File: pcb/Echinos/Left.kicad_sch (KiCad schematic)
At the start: 39 parts, among them J1 USB_C_Receptacle_USB2.0, J2 TagConnect_6pins, J206 Conn_01x06_Pin, J208 FPC (PCB), J301 SATA-7p, J4 FPC_VIK, SW1 SW_Push, SW2 SW_Push, U2 W25Q128JVS, U3 ESD7L5.0DT5G-N, U5 XC6210B332MR-G, U7 D3V3F4U6S-7

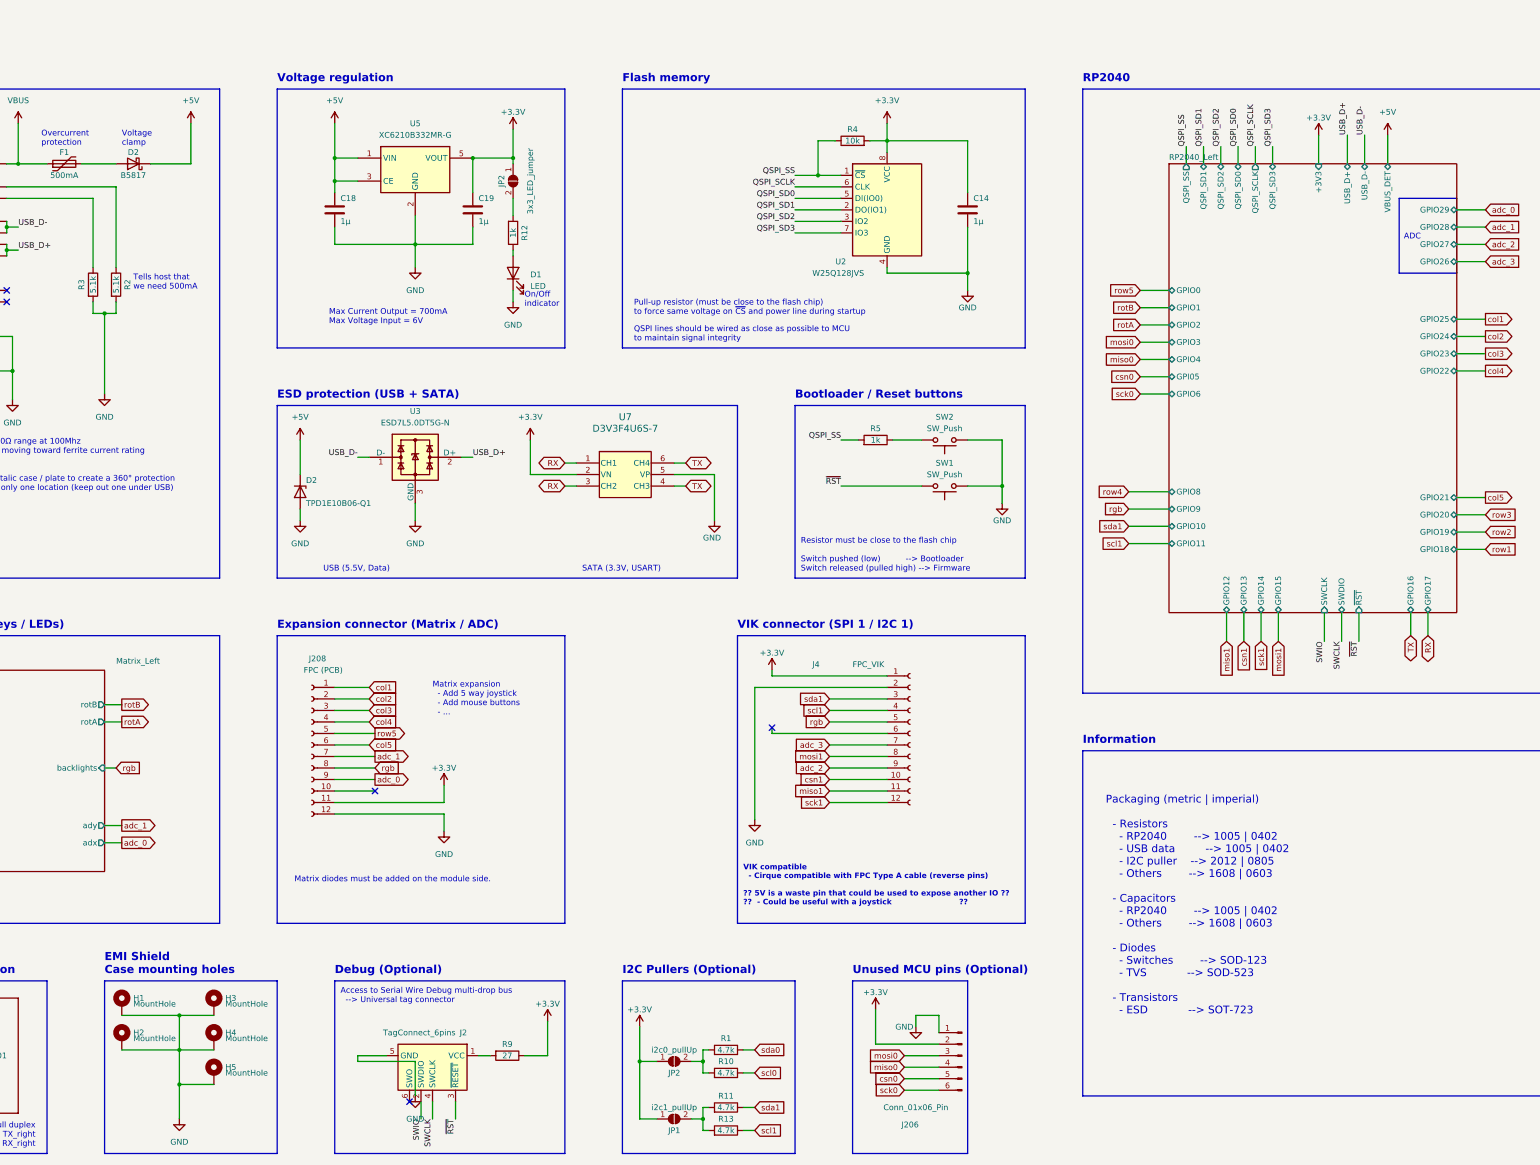
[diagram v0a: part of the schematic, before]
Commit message: 🚧 [PCB] - Backup before trying to add 5.0V support.
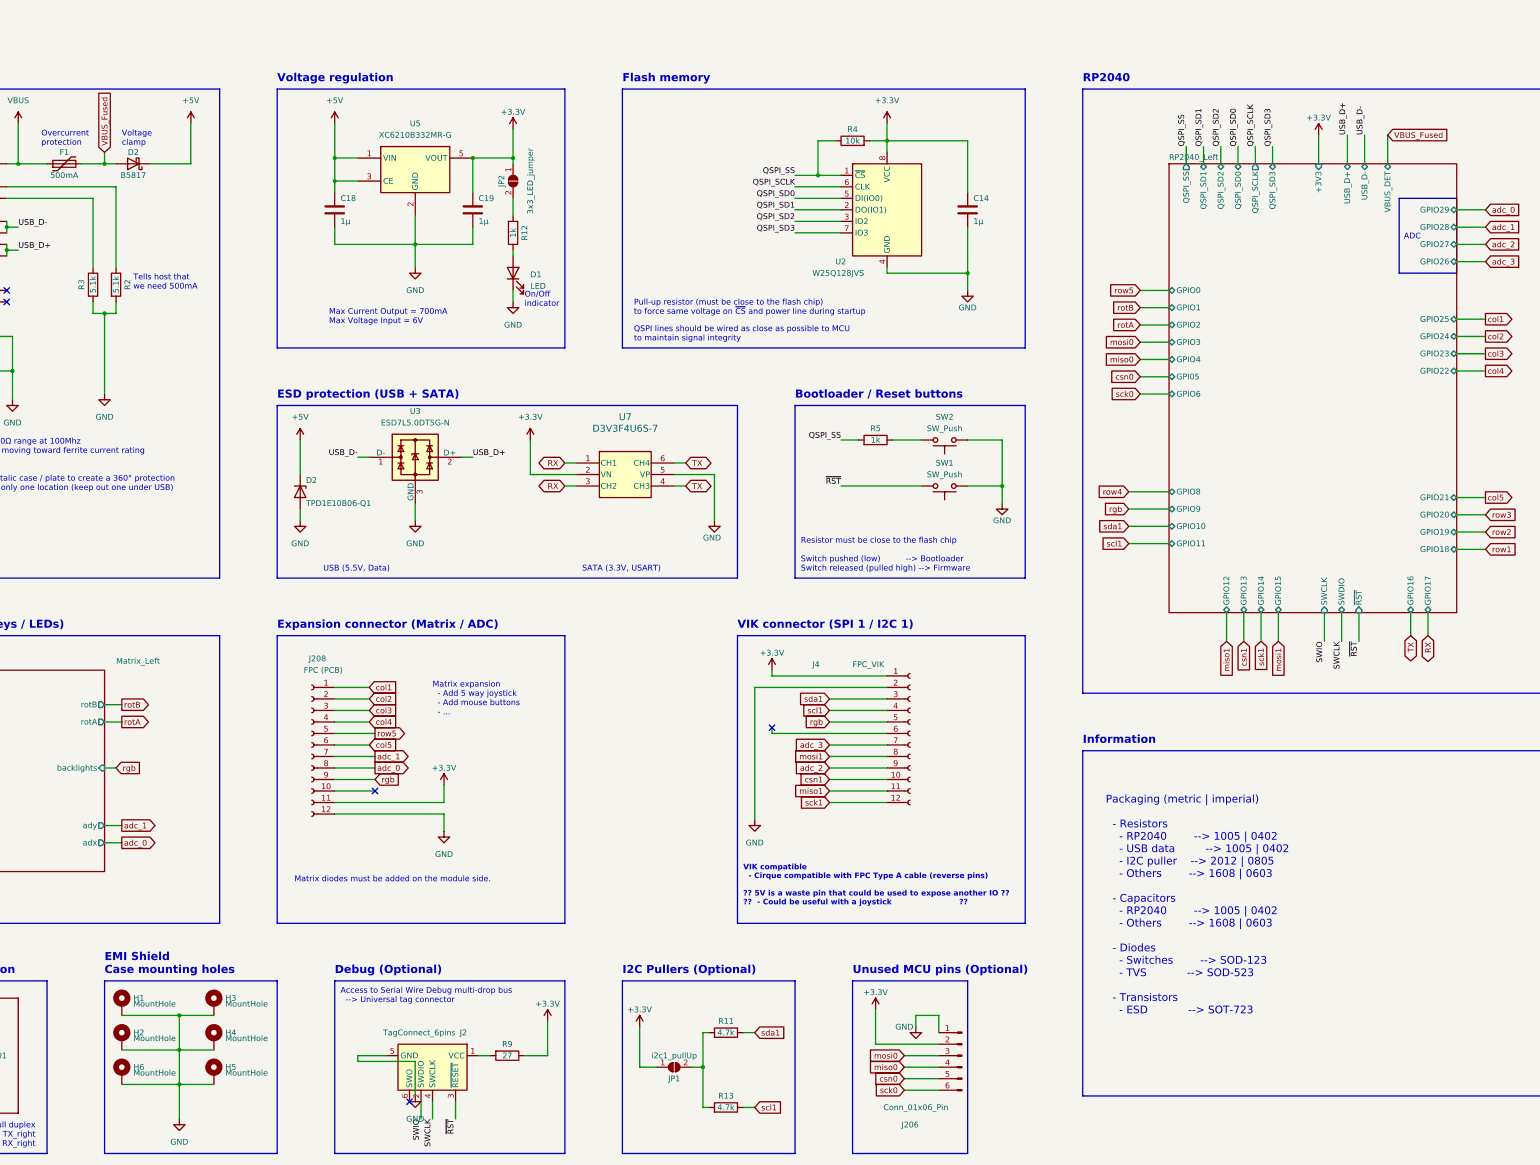
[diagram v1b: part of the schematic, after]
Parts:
- removed JP2: i2c0_pullUp, Echinos:SolderJumper_Open_0.8x1.2mm, symbol Jumper:SolderJumper_2_Open
- removed R1, R10: 4.7k, Resistor_SMD:R_0805_2012Metric_Pad1.20x1.40mm_HandSolder, symbol Device:R
- added H6: MountHole, Echinos:MountingHole_3mm_Pad_Via, symbol Mechanical:MountingHole_Pad
- J206: footprint Connector_PinHeader_2.54mm:PinHeader_1x06_P2.54mm_Vertical -> Connector_PinSocket_2.00mm:PinSocket_1x06_P2.00mm_Horizontal; now left out of the parts list
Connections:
- net GND: now also H6.1
- net adc_0: now also J208.8 (Pin_8); no longer J208.9 (Pin_9)
- net rgb: now also J208.9 (Pin_9); no longer J208.8 (Pin_8)
- net VBUS_Fused: now reaches D2.2 (A), F1.2
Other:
- moved on the sheet: JP1, R11, R13

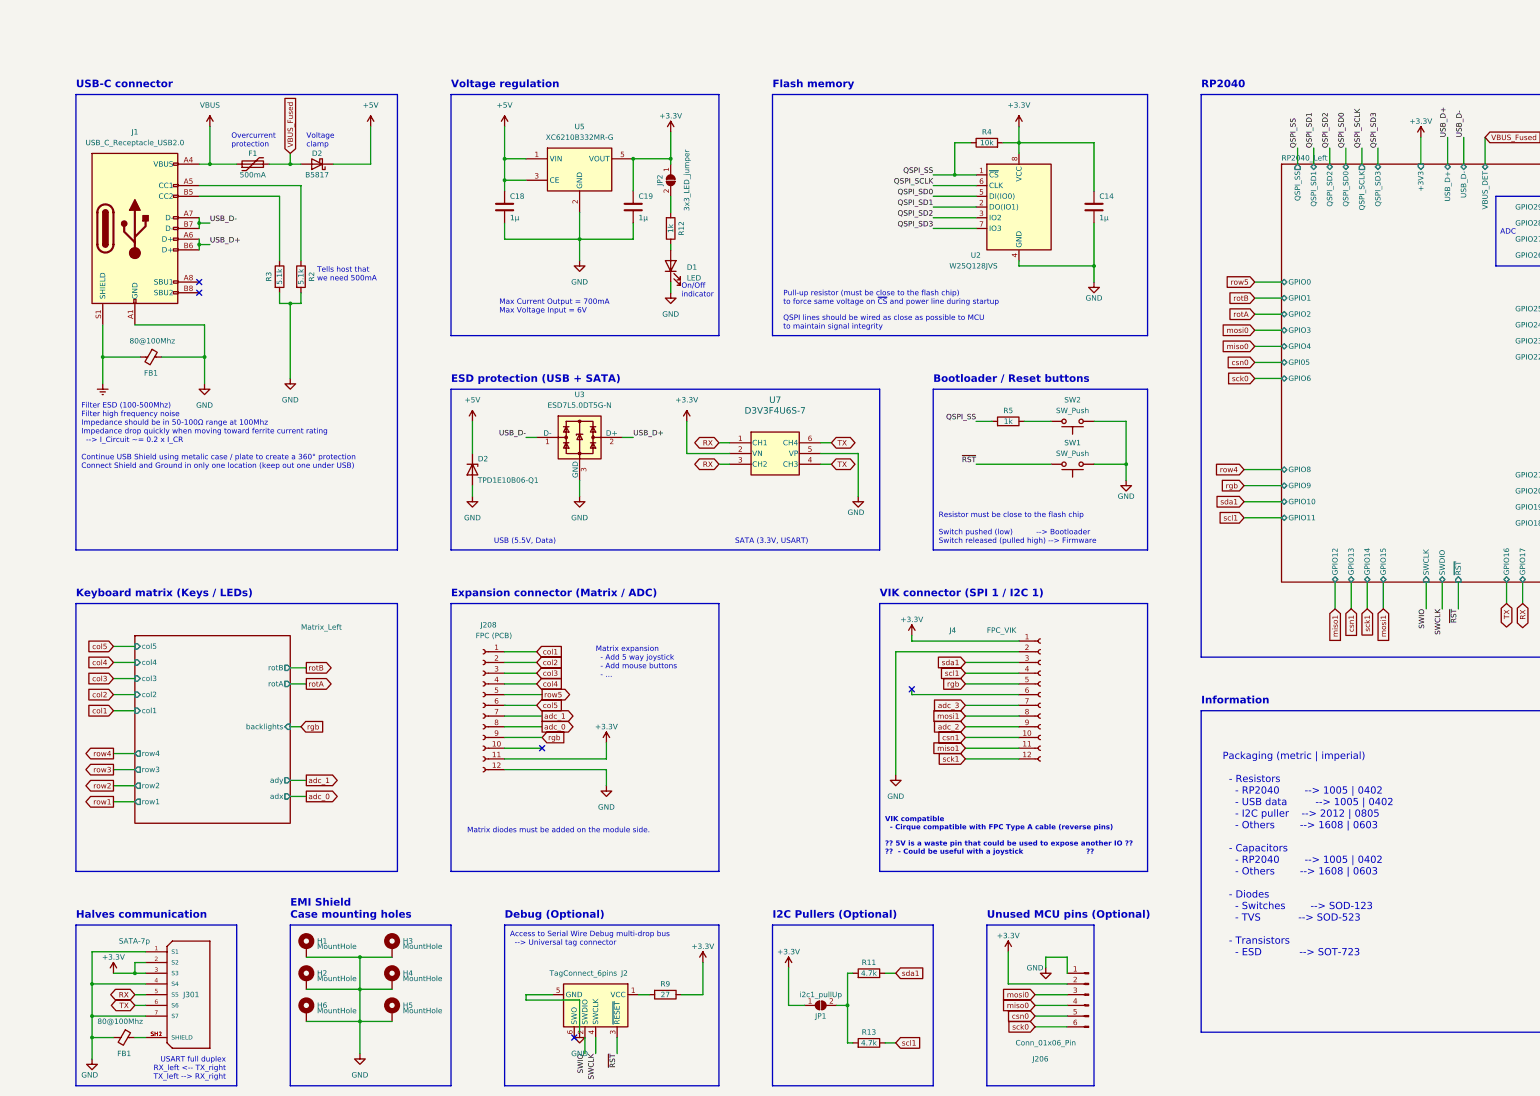
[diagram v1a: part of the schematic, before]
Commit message: ✨ 🚧 [PCB] - Halves are now connected with 5.0V power to be able to expose it to modules (see VIK standard). Update the whole routing to make this happens. VBUS and 5.0V are now split with a schottky diode to still be able to detect when USB is plugged but avoid reverse current in case power comes from the other half. Add ESD events protection to SATA connector.
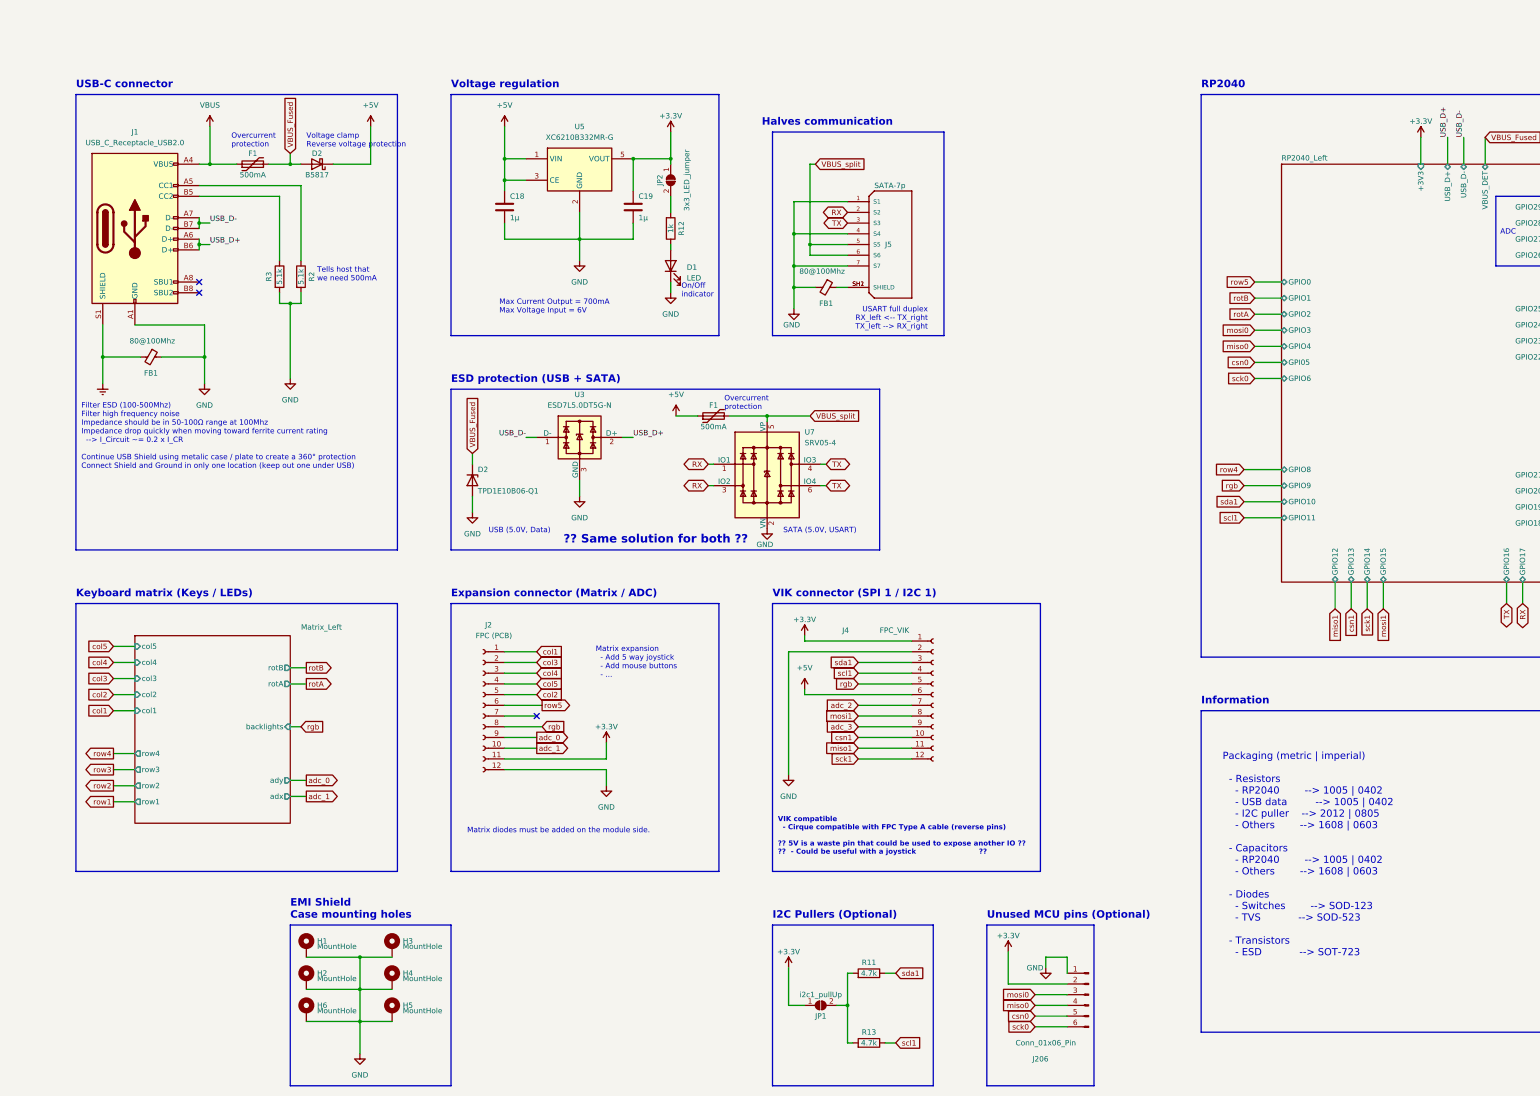
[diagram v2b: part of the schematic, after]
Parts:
- removed C14: 1µ, Capacitor_SMD:C_0603_1608Metric_Pad1.08x0.95mm_HandSolder, symbol Device:C
- removed J2: TagConnect_6pins, Connector:Tag-Connect_TC2030-IDC-FP_2x03_P1.27mm_Vertical, symbol Connector:Conn_ARM_SWD_TagConnect_TC2030
- removed R4: 10k, Resistor_SMD:R_0402_1005Metric_Pad0.72x0.64mm_HandSolder, symbol Device:R
- removed R5: 1k, Resistor_SMD:R_0402_1005Metric_Pad0.72x0.64mm_HandSolder, symbol Device:R
- removed R9: 27, Resistor_SMD:R_0402_1005Metric_Pad0.72x0.64mm_HandSolder, symbol Device:R
- removed SW1, SW2: SW_Push, Button_Switch_SMD:SW_SPST_CK_KXT3, symbol Switch:SW_Push
- removed U2: W25Q128JVS, Package_SO:SOIC-8_5.23x5.23mm_P1.27mm, symbol Memory_Flash:W25Q128JVS
- removed U7: D3V3F4U6S-7, Echinos:D_TVS_SOT-363, symbol Echinos:D3V3F4U6S-7
- added F1: 500mA, Fuse:Fuse_0603_1608Metric_Pad1.05x0.95mm_HandSolder, symbol Device:Polyfuse
- added U7: SRV05-4, Package_TO_SOT_SMD:SOT-23-6, symbol Power_Protection:SRV05-4
- renumbered J208 to J2, J301 to J5
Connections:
- net +3.3V: no longer J5.2 (S2), J5.3 (S3)
- net +5V: now also J4.6 (Pin_6), F1.1; no longer D2.1 (K)
- net GND: now also U7.2 (VN)
- net RX: now also J5.2 (S2), U7.1 (IO1), U7.3 (IO2); no longer J5.5 (S5)
- net TX: now also J5.3 (S3), U7.4 (IO3), U7.6 (IO4); no longer J5.6 (S6)
- net VBUS_Fused: now also D2.1 (K)
- net adc_0: now also J2.9 (Pin_9); no longer J2.8 (Pin_8)
- net adc_1: now also J2.10 (Pin_10); no longer J2.7 (Pin_7)
- net adc_2: now also J4.7 (Pin_7); no longer J4.9 (Pin_9)
- net adc_3: now also J4.9 (Pin_9); no longer J4.7 (Pin_7)
- net col2: now also J2.5 (Pin_5); no longer J2.2 (Pin_2)
- net col3: now also J2.2 (Pin_2); no longer J2.3 (Pin_3)
- net col4: now also J2.3 (Pin_3); no longer J2.4 (Pin_4)
- net col5: now also J2.4 (Pin_4); no longer J2.6 (Pin_6)
- net rgb: now also J2.8 (Pin_8); no longer J2.9 (Pin_9)
- net row5: now also J2.6 (Pin_6); no longer J2.5 (Pin_5)
- new net VBUS_split: F1.2, J5.5 (S5), J5.6 (S6), U7.5 (VP)
- no-connect marks 5 -> 3
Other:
- sheet RP2040_Left ports: added none; removed QSPI_SCLK, QSPI_SD0, QSPI_SD1, QSPI_SD2, QSPI_SD3, QSPI_SS, SWCLK, SWDIO, ~{RST}
- note added: "?? Same solution for both ??"
- note added: "SATA (5.0V, USART)"
- note added: "USB (5.0V, Data)"
- note added: "Voltage clamp Reverse voltage protection"
- note removed: "Access to Serial Wire Debug multi-drop bus --> Universal tag connector"
- note removed: "Bootloader / Reset buttons"
- note removed: "Debug (Optional)"
- note removed: "Flash memory"
- note removed: "Pull-up resistor (must be close to the flash chip) to force same voltage on ~{CS} and power line during startup"
- note removed: "QSPI lines should be wired as close as possible to MCU to maintain signal integrity"
- note removed: "Resistor must be close to the flash chip Switch pushed (low) --> Bootloader Switch released (pulled high) --> Firmware"
- note removed: "SATA (3.3V, USART)"
- note removed: "USB (5.5V, Data)"
- note removed: "Voltage clamp"
- moved on the sheet: D2, FB1, J4, J5
